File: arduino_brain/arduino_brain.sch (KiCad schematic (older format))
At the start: 53 parts, among them Q1 2N3904, Q10 2N3904, Q11 2N3906, Q2 TIP120, Q3 TIP120, Q4 2N3904, Q5 2N3906, Q6 2N3904, Q7 2N3906, Q8 2N3904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

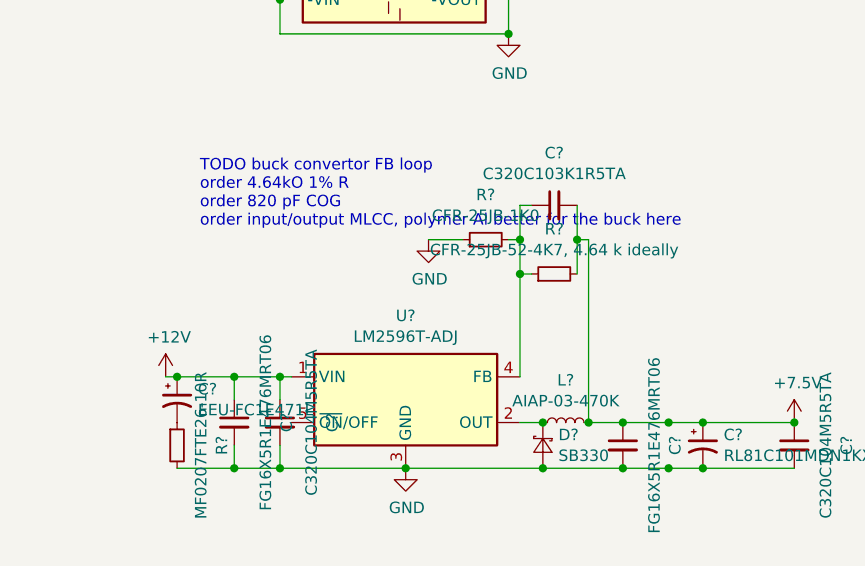
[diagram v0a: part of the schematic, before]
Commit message: 12 to 7 V stage on protoboard - 7V output confirmed!
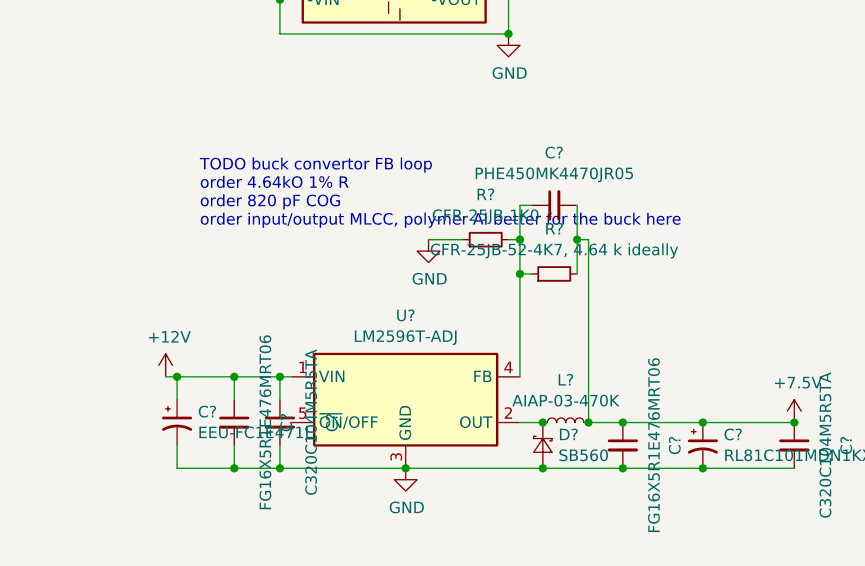
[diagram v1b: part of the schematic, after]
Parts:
- removed R?: MF0207FTE26-10R, symbol Device:R_Small
- C?: value C320C103K1R5TA -> PHE450MK4470JR05
- D?: value SB330 -> SB560
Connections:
- net -BATT: now also C?.2
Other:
- moved on the sheet: C?
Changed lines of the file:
@@
 L Device:CP1_Small C?
 U 1 1 5EA898FE
-P 600 10650
-F 0 "C?" H 691 10696 50  0000 L CNN
-F 1 "EEU-FC1E471L" H 691 10605 50  0000 L CNN
-F 2 "" H 600 10650 50  0001 C CNN
-F 3 "~" H 600 10650 50  0001 C CNN
-	1    600  10650
+P 600 10750
+F 0 "C?" H 691 10796 50  0000 L CNN
+F 1 "EEU-FC1E471L" H 691 10705 50  0000 L CNN
+F 2 "" H 600 10750 50  0001 C CNN
+F 3 "~" H 600 10750 50  0001 C CNN
+	1    600  10750
 	1    0    0    -1
 $EndComp
@@
 P 2250 9800
 F 0 "C?" V 2479 9800 50  0000 C CNN
-F 1 "C320C103K1R5TA" V 2388 9800 50  0000 C CNN
+F 1 "PHE450MK4470JR05" V 2388 9800 50  0000 C CNN
 F 2 "" H 2250 9800 50  0001 C CNN
 F 3 "~" H 2250 9800 50  0001 C CNN
@@
 P 2200 10850
 F 0 "D?" V 2154 10782 50  0000 R CNN
-F 1 "SB330" V 2245 10782 50  0000 R CNN
+F 1 "SB560" V 2245 10782 50  0000 R CNN
 F 2 "" V 2200 10850 50  0001 C CNN
 F 3 "~" V 2200 10850 50  0001 C CNN
@@
 	2400 10750 2550 10750
 Connection ~ 2400 10750
-Connection ~ 2750 10750
 Wire Wire Line
 	2200 10950 2550 10950
 Connection ~ 2200 10950
-Connection ~ 2750 10950
 $Comp
 L power:+7.5V #PWR?
@@
 	600  10550 850  10550
 $Comp
-L Device:R_Small R?
-U 1 1 5E3F5204
-P 600 10850
-F 0 "R?" V 796 10850 50  0000 C CNN
-F 1 "MF0207FTE26-10R" V 705 10850 50  0000 C CNN
-F 2 "" H 600 10850 50  0001 C CNN
-F 3 "~" H 600 10850 50  0001 C CNN
-	1    600  10850
-	1    0    0    -1
-$EndComp
-$Comp
 L Device:C_Small C?
 U 1 1 5E40EDD4
@@
 Connection ~ 2550 10750
 Connection ~ 2550 10950
-Wire Wire Line
-	2750 10750 2900 10750
-Wire Wire Line
-	2750 10950 2900 10950
 Connection ~ 2900 10750
 Wire Wire Line
@@
 	2900 10950 3300 10950
 Wire Wire Line
-	2550 10950 2750 10950
-Wire Wire Line
-	2550 10750 2750 10750
+	2550 10750 2900 10750
+Wire Wire Line
+	2550 10950 2900 10950
+Wire Wire Line
+	600  10850 600  10950
+Wire Wire Line
+	600  10650 600  10550
 $EndSCHEMATC

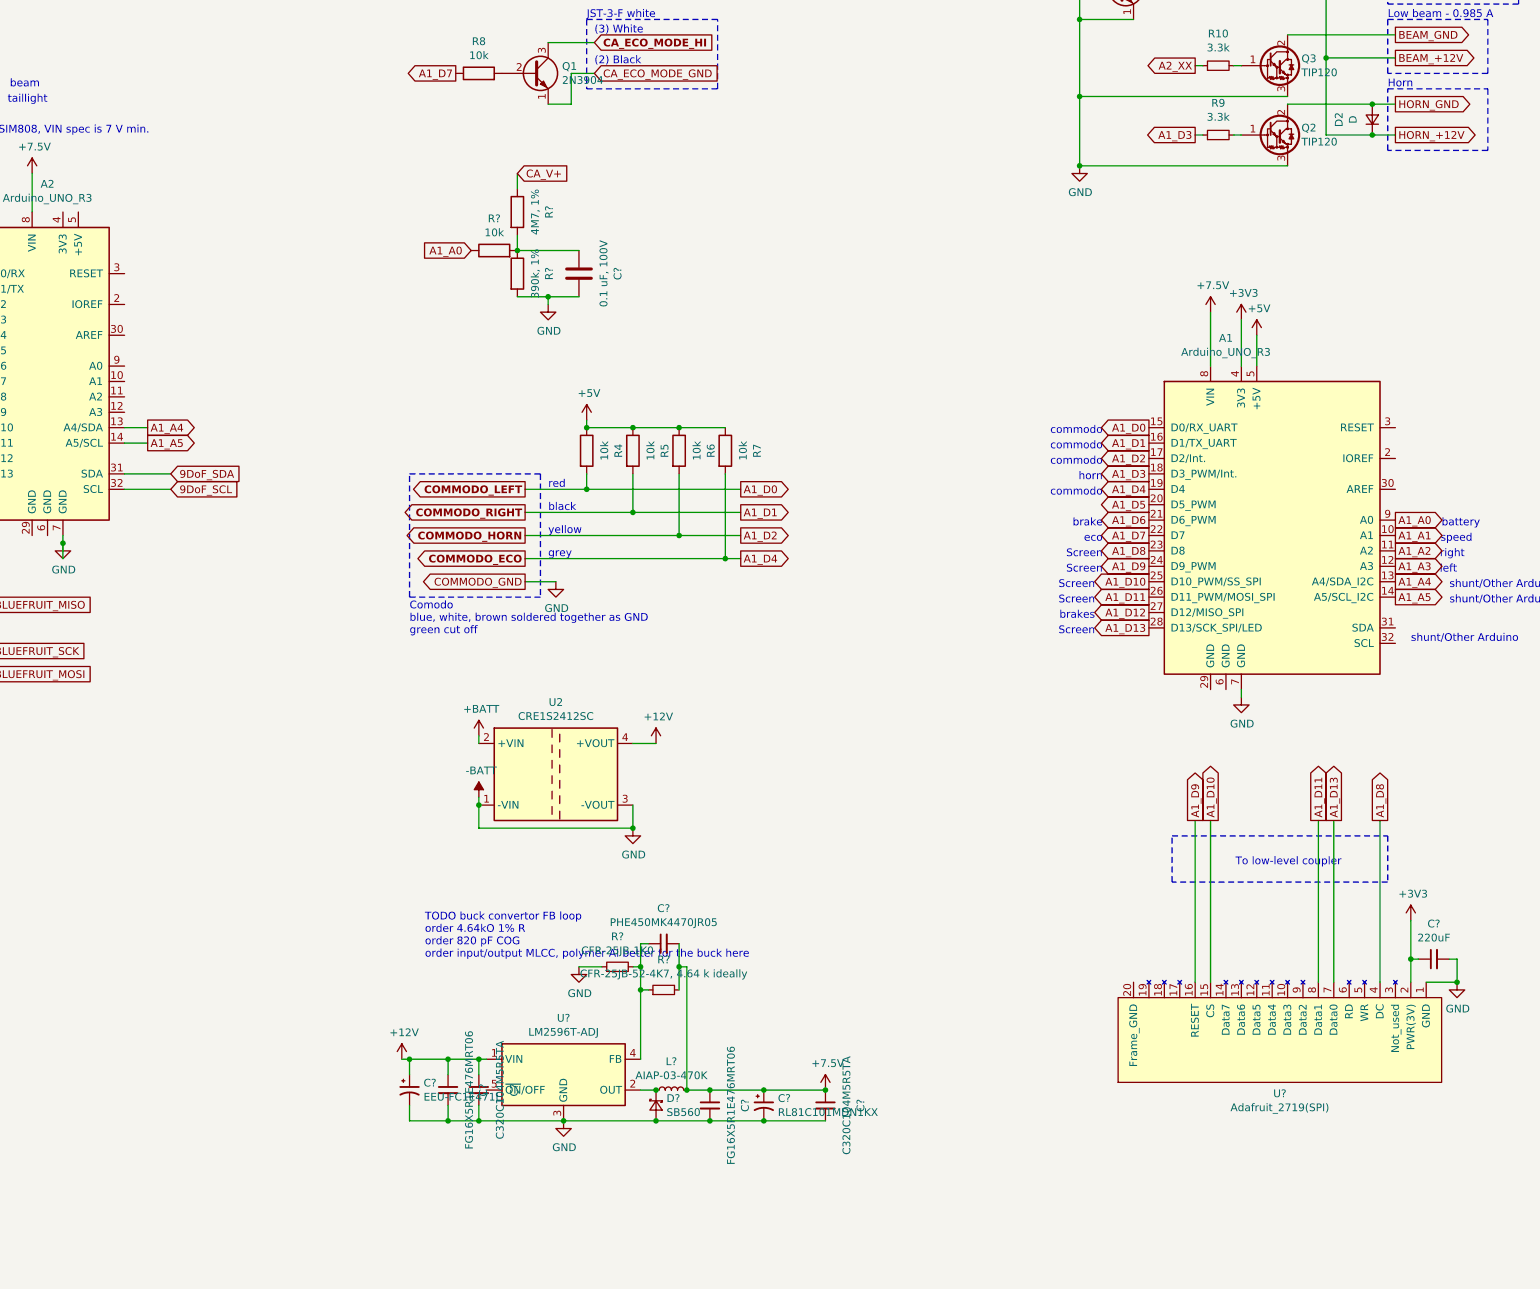
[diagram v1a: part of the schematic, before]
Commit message: Included thermal characteristics of 12 to 7 V stage
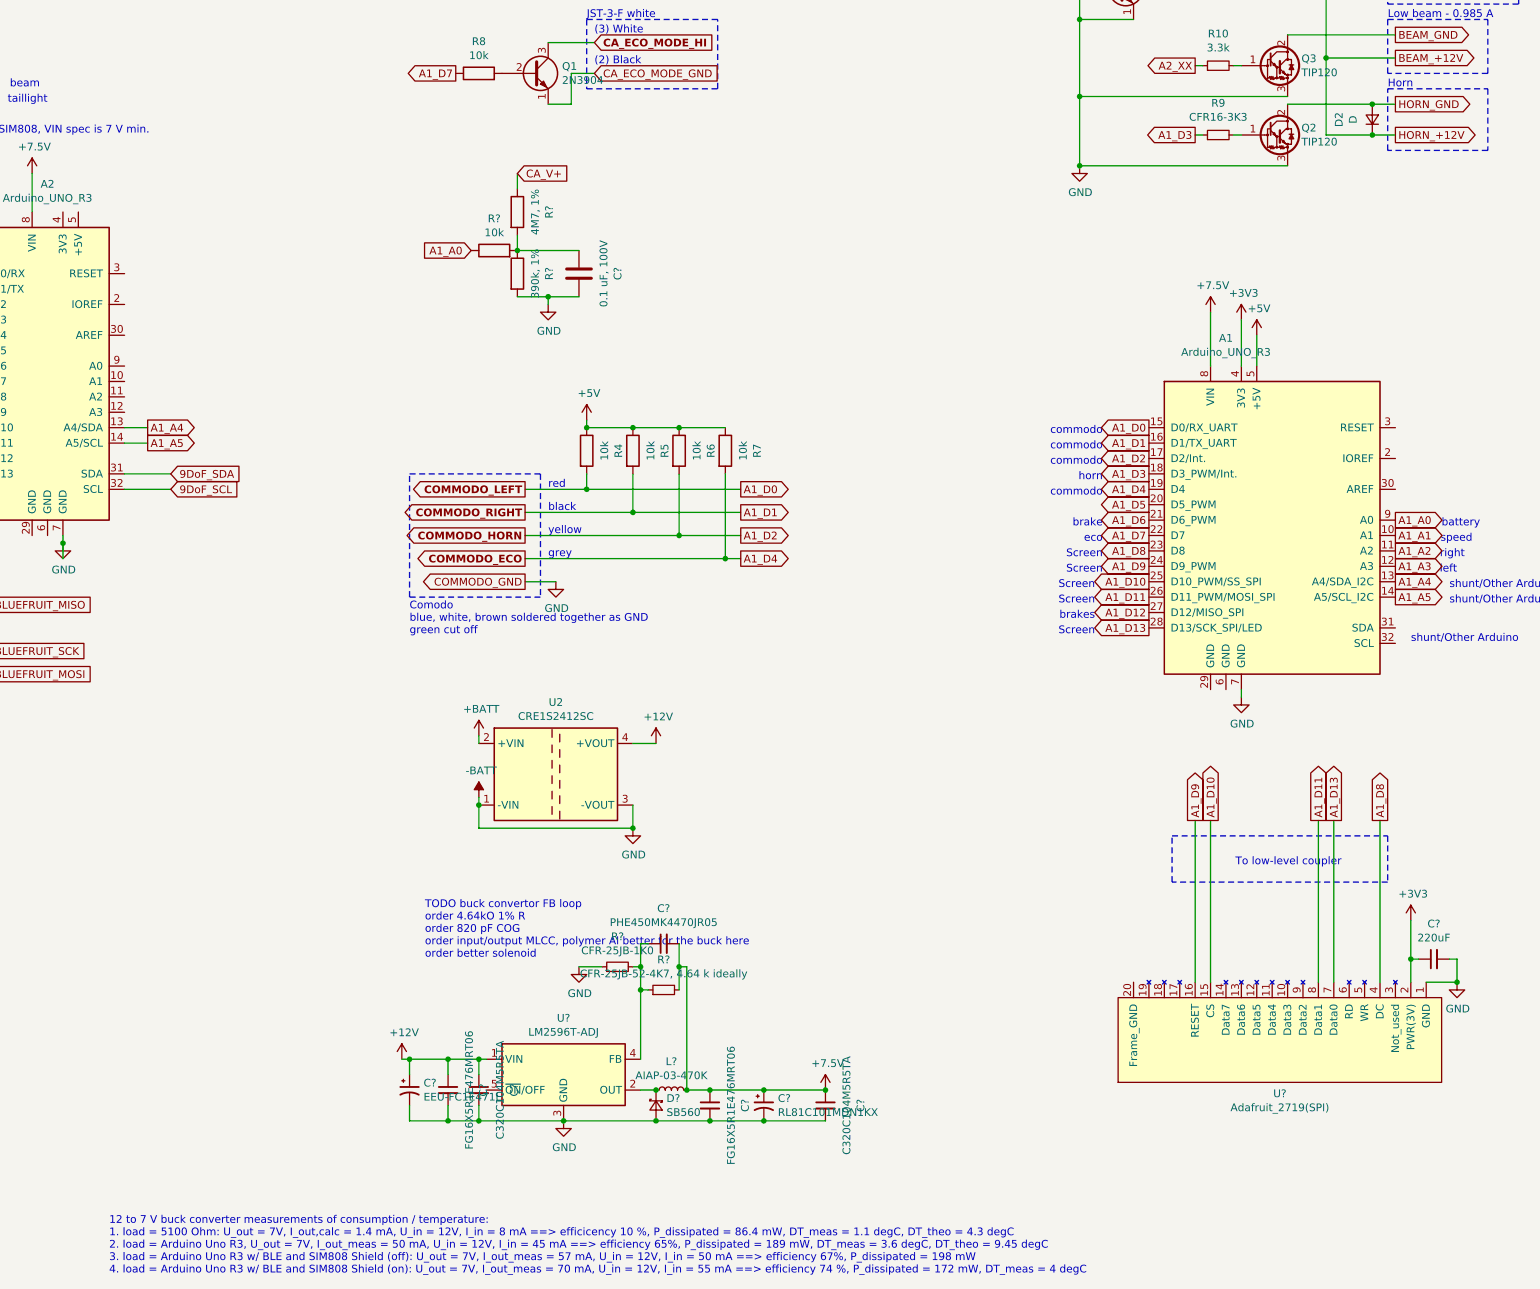
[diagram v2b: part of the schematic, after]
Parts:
- R9: value 3.3k -> CFR16-3K3
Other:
- note added: "12 to 7 V buck converter measurements of consumption / temperature:\n1. load = 5100 Ohm: U_out = 7V, I_out,calc = 1.4 mA, U_in = 12V, I_in = 8 mA ==> efficicency 10 %, P_dissipated = 86.4 mW, DT_meas = 1.1 degC, DT_theo = 4.3 degC\n2. load = Arduino Uno R3, U_out = 7V, I_out_meas = 50 mA, U_in = 12V, I_in = 45 mA ==> efficiency 65%, P_dissipated = 189 mW, DT_meas = 3.6 degC, DT_theo = 9.45 degC\n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"
- note added: "TODO buck convertor FB loop\norder 4.64kO 1% R\norder 820 pF COG\norder input/output MLCC, polymer Al better for the buck here\norder better solenoid"
- note removed: "TODO buck convertor FB loop\norder 4.64kO 1% R\norder 820 pF COG\norder input/output MLCC, polymer Al better for the buck here"
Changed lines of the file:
@@
 P 5850 4550
 F 0 "R9" V 6057 4550 50  0000 C CNN
-F 1 "3.3k" V 5966 4550 50  0000 C CNN
+F 1 "CFR16-3K3" V 5966 4550 50  0000 C CNN
 F 2 "" V 5780 4550 50  0001 C CNN
 F 3 "~" H 5850 4550 50  0001 C CNN
@@
 $EndComp
 Text Notes 700  9900 0    50   ~ 0
-TODO buck convertor FB loop\norder 4.64kO 1% R\norder 820 pF COG\norder input/output MLCC, polymer Al better for the buck here
+TODO buck convertor FB loop\norder 4.64kO 1% R\norder 820 pF COG\norder input/output MLCC, polymer Al better for the buck here\norder better solenoid
 Connection ~ 1050 10950
 Wire Wire Line
@@
 Wire Wire Line
 	600  10650 600  10550
+Text Notes -1350 11950 0    50   ~ 0
+12 to 7 V buck converter measurements of consumption / temperature:\n1. load = 5100 Ohm: U_out = 7V, I_out,calc = 1.4 mA, U_in = 12V, I_in = 8 mA ==> efficicency 10 %, P_dissipated = 86.4 mW, DT_meas = 1.1 degC, DT_theo = 4.3 degC\n2. load = Arduino Uno R3, U_out = 7V, I_out_meas = 50 mA, U_in = 12V, I_in = 45 mA ==> efficiency 65%, P_dissipated = 189 mW, DT_meas = 3.6 degC, DT_theo = 9.45 degC\n3. load = Arduino Uno R3 w/ BLE and SIM808 Shield (off): U_out = 7V, I_out_meas = 57 mA, U_in = 12V, I_in = 50 mA ==> efficiency 67%, P_dissipated = 198 mW\n4. load = Arduino Uno R3 w/ BLE and SIM808 Shield (on): U_out = 7V, I_out_meas = 70 mA, U_in = 12V, I_in = 55 mA ==> efficiency 74 %, P_dissipated = 172 mW, DT_meas = 4 degC
 $EndSCHEMATC

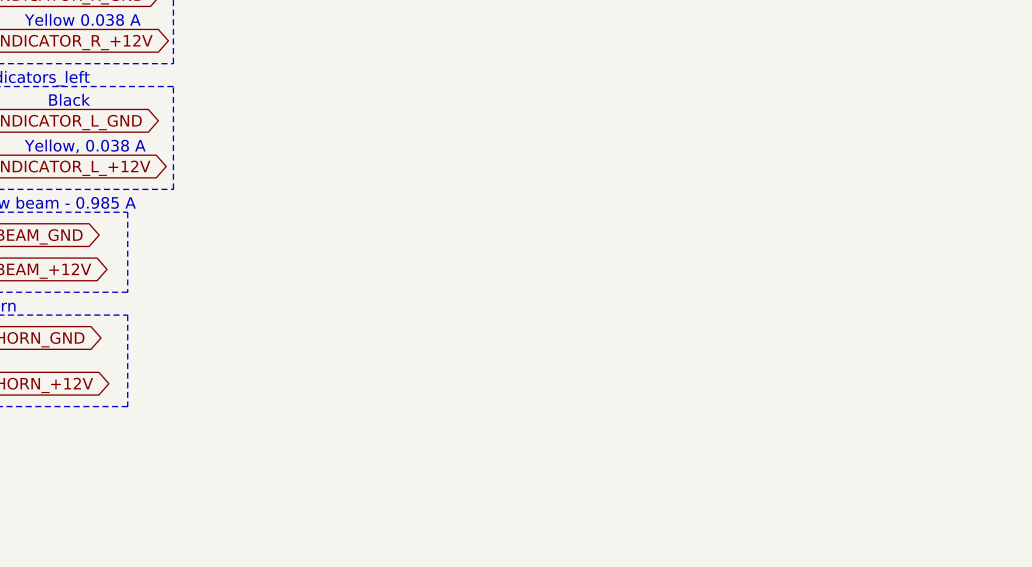
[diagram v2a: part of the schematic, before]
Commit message: Implemented horn circuit on breadboard. Working, but multimeter cannot read voltage drop.
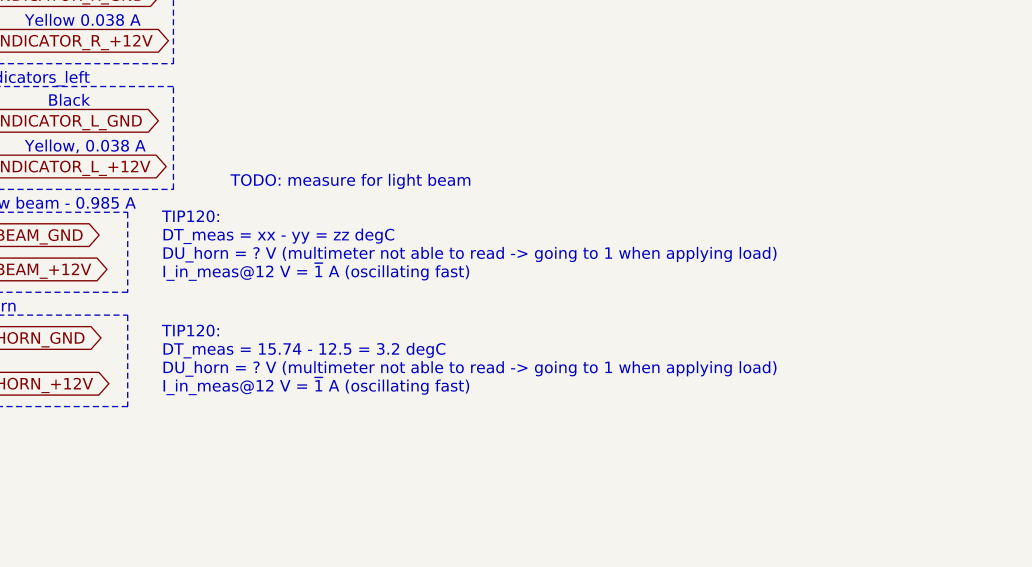
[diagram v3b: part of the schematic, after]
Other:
- note added: "TIP120:\nDT_meas = 15.74 - 12.5 = 3.2 degC\nDU_horn = ? V (multimeter not able to read -> going to 1 when applying load)\nI_in_meas@12 V = ~1 A (oscillating fast)"
- note added: "TIP120:\nDT_meas = xx - yy = zz degC\nDU_horn = ? V (multimeter not able to read -> going to 1 when applying load)\nI_in_meas@12 V = ~1 A (oscillating fast)"
- note added: "TODO: measure for light beam"
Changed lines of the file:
@@
 Text Notes -1350 11950 0    50   ~ 0
 12 to 7 V buck converter measurements of consumption / temperature:\n1. load = 5100 Ohm: U_out = 7V, I_out,calc = 1.4 mA, U_in = 12V, I_in = 8 mA ==> efficicency 10 %, P_dissipated = 86.4 mW, DT_meas = 1.1 degC, DT_theo = 4.3 degC\n2. load = Arduino Uno R3, U_out = 7V, I_out_meas = 50 mA, U_in = 12V, I_in = 45 mA ==> efficiency 65%, P_dissipated = 189 mW, DT_meas = 3.6 degC, DT_theo = 9.45 degC\n3. load = Arduino Uno R3 w/ BLE and SIM808 Shield (off): U_out = 7V, I_out_meas = 57 mA, U_in = 12V, I_in = 50 mA ==> efficiency 67%, P_dissipated = 198 mW\n4. load = Arduino Uno R3 w/ BLE and SIM808 Shield (on): U_out = 7V, I_out_meas = 70 mA, U_in = 12V, I_in = 55 mA ==> efficiency 74 %, P_dissipated = 172 mW, DT_meas = 4 degC
+Text Notes 7750 4600 0    50   ~ 0
+TIP120:\nDT_meas = 15.74 - 12.5 = 3.2 degC\nDU_horn = ? V (multimeter not able to read -> going to 1 when applying load)\nI_in_meas@12 V = ~1 A (oscillating fast)
+Text Notes 8050 3700 0    50   ~ 0
+TODO: measure for light beam
+Text Notes 7750 4100 0    50   ~ 0
+TIP120:\nDT_meas = xx - yy = zz degC\nDU_horn = ? V (multimeter not able to read -> going to 1 when applying load)\nI_in_meas@12 V = ~1 A (oscillating fast)
 $EndSCHEMATC
